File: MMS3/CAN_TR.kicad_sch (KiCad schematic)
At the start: 6 parts, among them U500 TJA1044GTK_3Z

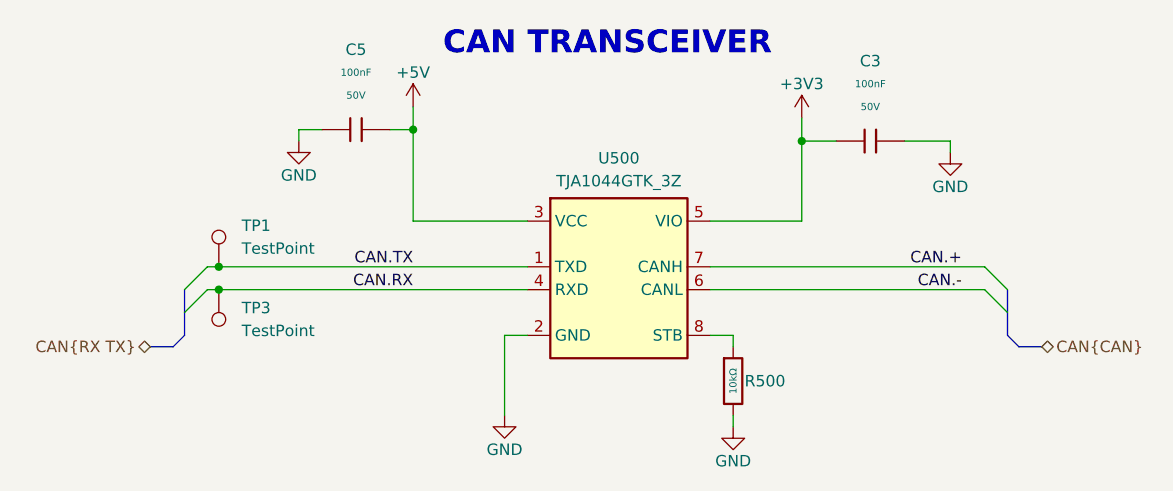
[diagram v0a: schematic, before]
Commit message: changed most of stuff to ch32L103
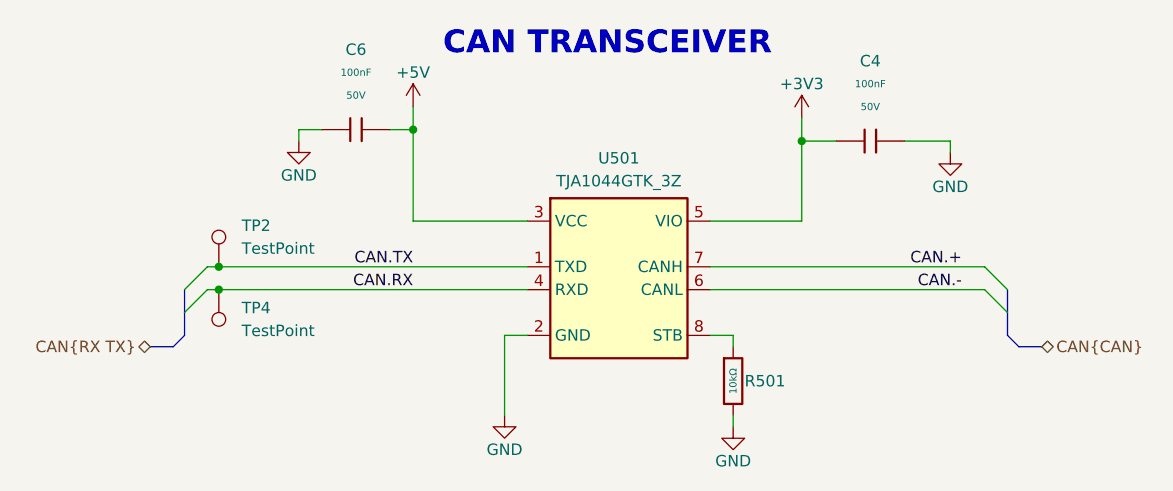
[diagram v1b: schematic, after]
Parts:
- renumbered C3 to C4, C5 to C6, R500 to R501, TP1 to TP2, TP3 to TP4, U500 to U501
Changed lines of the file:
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@@
 		(in_pos_files yes)
 		(dnp no)
-		(property "Reference" "R500"
+		(property "Reference" "R501"
 			(at 180.34 113.03 0)
 			(show_name no)
@@
 				(path "/712cea22-140d-4c92-923f-f4998caf3ecd/307a68f1-f486-4a0f-b1cd-0d4ec3697ff2"
 					(reference "R501")
-					(unit 1)
-				)
-				(path "/712cea22-140d-4c92-923f-f4998caf3ecd/8329e181-fea6-43ec-bb30-963882d9c26d"
-					(reference "R500")
 					(unit 1)
 				)
@@
 		(dnp no)
 		(fields_autoplaced yes)
-		(property "Reference" "C3"
+		(property "Reference" "C4"
 			(at 194.31 77.47 90)
 			(show_name no)
@@
 				(path "/712cea22-140d-4c92-923f-f4998caf3ecd/307a68f1-f486-4a0f-b1cd-0d4ec3697ff2"
 					(reference "C4")
-					(unit 1)
-				)
-				(path "/712cea22-140d-4c92-923f-f4998caf3ecd/8329e181-fea6-43ec-bb30-963882d9c26d"
-					(reference "C3")
 					(unit 1)
 				)
@@
 		(in_pos_files yes)
 		(dnp no)
-		(property "Reference" "#PWR0503"
+		(property "Reference" "#PWR0511"
 			(at 203.2 93.98 0)
 			(hide yes)
@@
 				(path "/712cea22-140d-4c92-923f-f4998caf3ecd/307a68f1-f486-4a0f-b1cd-0d4ec3697ff2"
 					(reference "#PWR0511")
-					(unit 1)
-				)
-				(path "/712cea22-140d-4c92-923f-f4998caf3ecd/8329e181-fea6-43ec-bb30-963882d9c26d"
-					(reference "#PWR0503")
 					(unit 1)
 				)
@@
 		(dnp no)
 		(fields_autoplaced yes)
-		(property "Reference" "TP3"
+		(property "Reference" "TP4"
 			(at 124.46 104.9019 0)
 			(show_name no)
@@
 				(path "/712cea22-140d-4c92-923f-f4998caf3ecd/307a68f1-f486-4a0f-b1cd-0d4ec3697ff2"
 					(reference "TP4")
-					(unit 1)
-				)
-				(path "/712cea22-140d-4c92-923f-f4998caf3ecd/8329e181-fea6-43ec-bb30-963882d9c26d"
-					(reference "TP3")
 					(unit 1)
 				)
@@
 		(dnp no)
 		(fields_autoplaced yes)
-		(property "Reference" "C5"
+		(property "Reference" "C6"
 			(at 137.16 76.2 90)
 			(show_name no)
@@
 				(path "/712cea22-140d-4c92-923f-f4998caf3ecd/307a68f1-f486-4a0f-b1cd-0d4ec3697ff2"
 					(reference "C6")
-					(unit 1)
-				)
-				(path "/712cea22-140d-4c92-923f-f4998caf3ecd/8329e181-fea6-43ec-bb30-963882d9c26d"
-					(reference "C5")
 					(unit 1)
 				)
@@
 		(in_pos_files yes)
 		(dnp no)
-		(property "Reference" "U500"
+		(property "Reference" "U501"
 			(at 166.37 88.265 0)
 			(show_name no)
@@
 				(path "/712cea22-140d-4c92-923f-f4998caf3ecd/307a68f1-f486-4a0f-b1cd-0d4ec3697ff2"
 					(reference "U501")
-					(unit 1)
-				)
-				(path "/712cea22-140d-4c92-923f-f4998caf3ecd/8329e181-fea6-43ec-bb30-963882d9c26d"
-					(reference "U500")
 					(unit 1)
 				)
@@
 		(in_pos_files yes)
 		(dnp no)
-		(property "Reference" "#PWR0504"
+		(property "Reference" "#PWR0508"
 			(at 153.67 123.19 0)
 			(hide yes)
@@
 				(path "/712cea22-140d-4c92-923f-f4998caf3ecd/307a68f1-f486-4a0f-b1cd-0d4ec3697ff2"
 					(reference "#PWR0508")
-					(unit 1)
-				)
-				(path "/712cea22-140d-4c92-923f-f4998caf3ecd/8329e181-fea6-43ec-bb30-963882d9c26d"
-					(reference "#PWR0504")
 					(unit 1)
 				)
@@
 		(dnp no)
 		(fields_autoplaced yes)
-		(property "Reference" "TP1"
+		(property "Reference" "TP2"
 			(at 124.46 95.7579 0)
 			(show_name no)
@@
 				(path "/712cea22-140d-4c92-923f-f4998caf3ecd/307a68f1-f486-4a0f-b1cd-0d4ec3697ff2"
 					(reference "TP2")
-					(unit 1)
-				)
-				(path "/712cea22-140d-4c92-923f-f4998caf3ecd/8329e181-fea6-43ec-bb30-963882d9c26d"
-					(reference "TP1")
 					(unit 1)
 				)
@@
 		(in_pos_files yes)
 		(dnp no)
-		(property "Reference" "#PWR0505"
+		(property "Reference" "#PWR0510"
 			(at 179.07 124.46 0)
 			(hide yes)
@@
 				(path "/712cea22-140d-4c92-923f-f4998caf3ecd/307a68f1-f486-4a0f-b1cd-0d4ec3697ff2"
 					(reference "#PWR0510")
-					(unit 1)
-				)
-				(path "/712cea22-140d-4c92-923f-f4998caf3ecd/8329e181-fea6-43ec-bb30-963882d9c26d"
-					(reference "#PWR0505")
 					(unit 1)
 				)
@@
 		(in_pos_files yes)
 		(dnp no)
-		(property "Reference" "#PWR0501"
+		(property "Reference" "#PWR0509"
 			(at 186.69 87.63 0)
 			(hide yes)
@@
 				(path "/712cea22-140d-4c92-923f-f4998caf3ecd/307a68f1-f486-4a0f-b1cd-0d4ec3697ff2"
 					(reference "#PWR0509")
-					(unit 1)
-				)
-				(path "/712cea22-140d-4c92-923f-f4998caf3ecd/8329e181-fea6-43ec-bb30-963882d9c26d"
-					(reference "#PWR0501")
 					(unit 1)
 				)
@@
 		(in_pos_files yes)
 		(dnp no)
-		(property "Reference" "#PWR0500"
+		(property "Reference" "#PWR0507"
 			(at 143.51 86.36 0)
 			(hide yes)
@@
 				(path "/712cea22-140d-4c92-923f-f4998caf3ecd/307a68f1-f486-4a0f-b1cd-0d4ec3697ff2"
 					(reference "#PWR0507")
-					(unit 1)
-				)
-				(path "/712cea22-140d-4c92-923f-f4998caf3ecd/8329e181-fea6-43ec-bb30-963882d9c26d"
-					(reference "#PWR0500")
 					(unit 1)
 				)
@@
 		(in_pos_files yes)
 		(dnp no)
-		(property "Reference" "#PWR0502"
+		(property "Reference" "#PWR0506"
 			(at 130.81 92.71 0)
 			(hide yes)
@@
 					(unit 1)
 				)
-				(path "/712cea22-140d-4c92-923f-f4998caf3ecd/8329e181-fea6-43ec-bb30-963882d9c26d"
-					(reference "#PWR0502")
-					(unit 1)
-				)
